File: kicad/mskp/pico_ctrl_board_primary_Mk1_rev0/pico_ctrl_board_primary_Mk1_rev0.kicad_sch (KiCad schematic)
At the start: 12 parts, among them J1 Conn_01x06_Socket, J4 USB_C_Receptacle_USB2.0, J7 OLED_128x64, J8 Conn_01x12_Socket, J9 Conn_01x03_Socket, SW3 SW_Omron_B3FS, U1 Raspberry_Pi_Pico

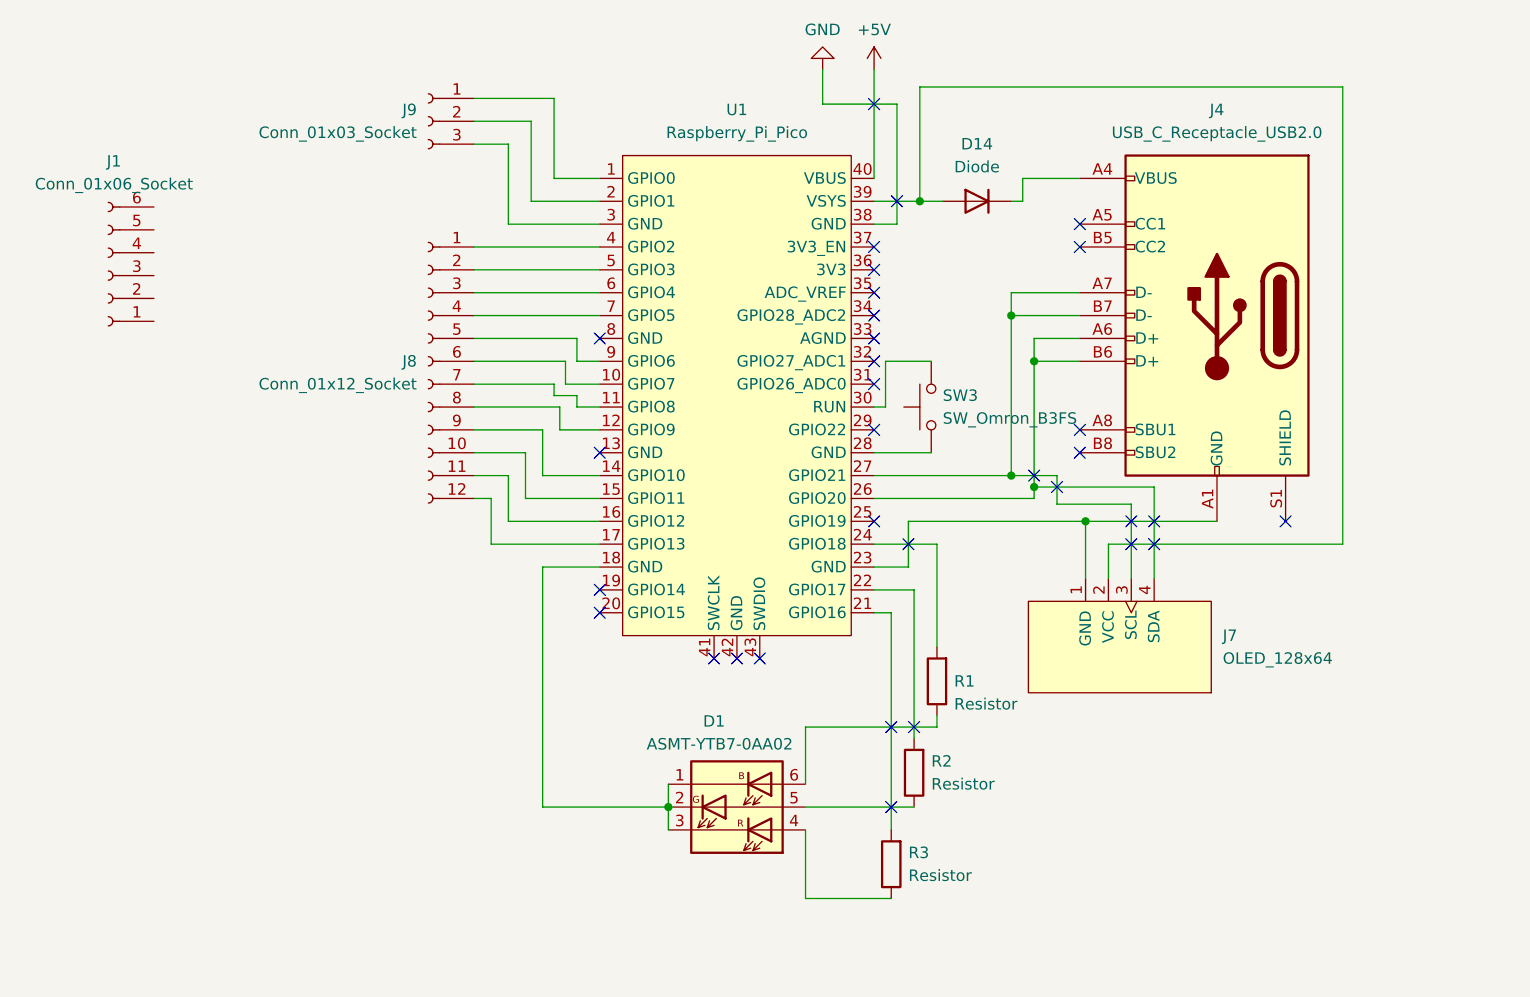
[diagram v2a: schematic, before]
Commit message: More work on pico layout and start of io shema layout
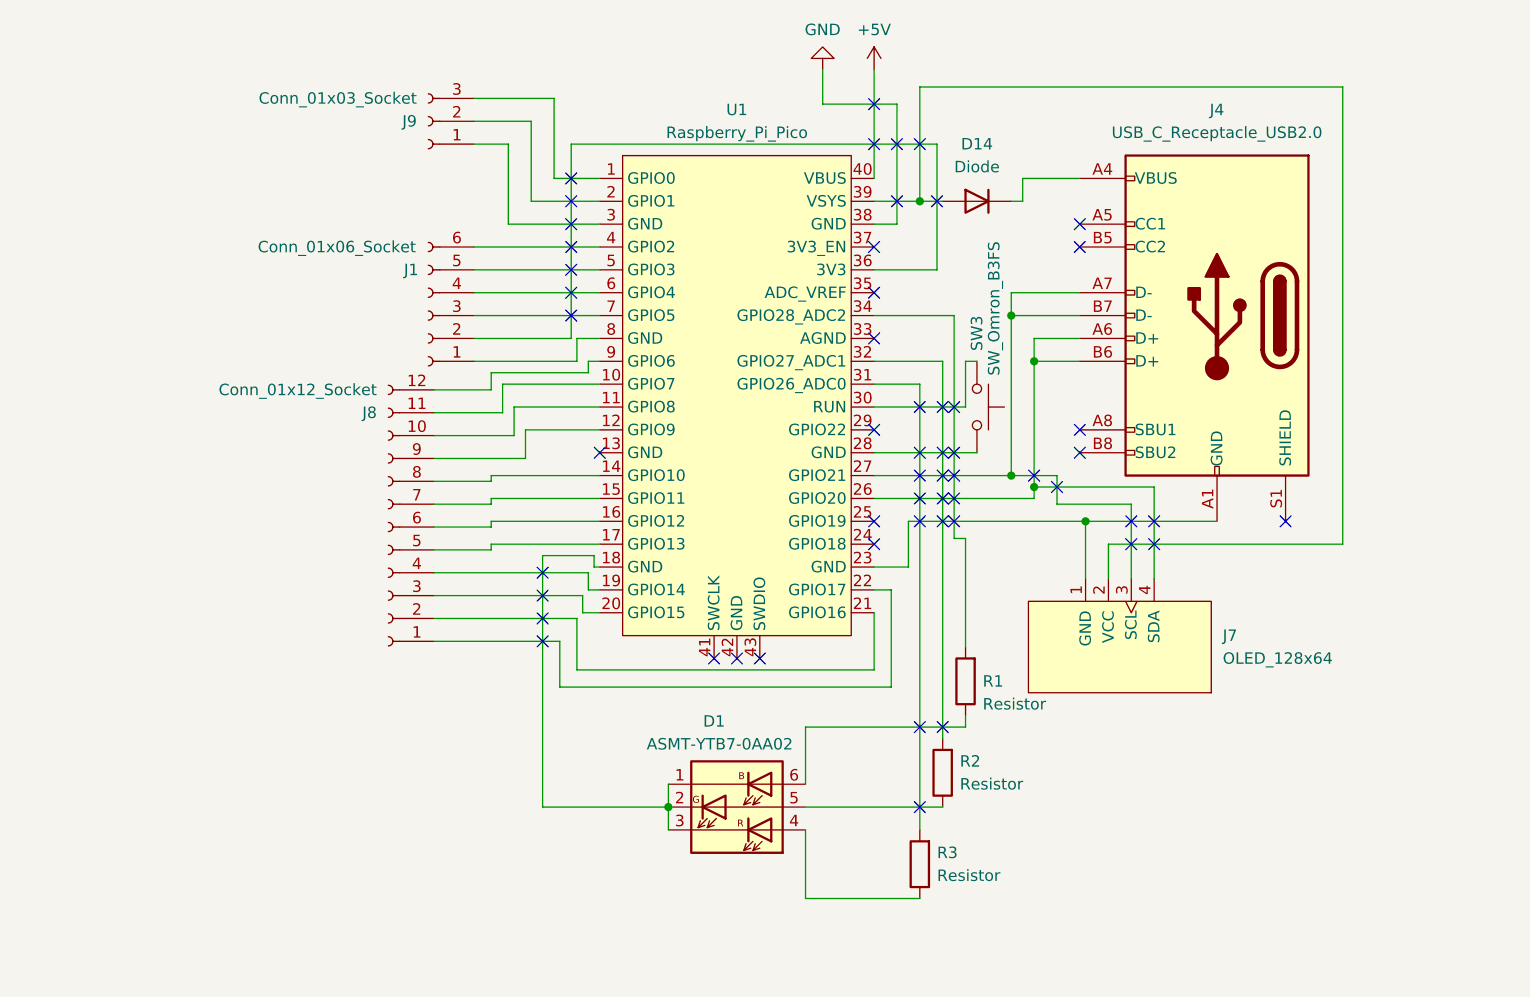
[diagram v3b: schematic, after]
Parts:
- J1: footprint (none) -> Connector_JST:JST_SH_SM06B-SRSS-TB_1x06-1MP_P1.00mm_Horizontal
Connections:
- net at U1.1 (GPIO0): now also J9.3 (Pin_3); no longer J9.1 (Pin_1)
- net at U1.10 (GPIO7): now also J8.11 (Pin_11); no longer J8.6 (Pin_6)
- net at U1.11 (GPIO8): now also J8.10 (Pin_10); no longer J8.7 (Pin_7)
- net at U1.12 (GPIO9): now also J8.9 (Pin_9); no longer J8.8 (Pin_8)
- net at U1.14 (GPIO10): now also J8.8 (Pin_8); no longer J8.9 (Pin_9)
- net at U1.15 (GPIO11): now also J8.7 (Pin_7); no longer J8.10 (Pin_10)
- net at U1.16 (GPIO12): now also J8.6 (Pin_6); no longer J8.11 (Pin_11)
- net at U1.17 (GPIO13): now also J8.5 (Pin_5); no longer J8.12 (Pin_12)
- net at U1.19 (GPIO14): now also J8.4 (Pin_4)
- net at U1.20 (GPIO15): now also J8.3 (Pin_3)
- net at U1.21 (GPIO16): now also J8.2 (Pin_2); no longer R3.2
- net at U1.22 (GPIO17): now also J8.1 (Pin_1); no longer R2.2
- net at U1.24 (GPIO18): no longer R1.2
- net at U1.3 (GND): now also J9.1 (Pin_1); no longer J9.3 (Pin_3)
- net at U1.31 (GPIO26_ADC0): now also R3.2
- net at U1.32 (GPIO27_ADC1): now also R2.2
- net at U1.34 (GPIO28_ADC2): now also R1.2
- net at U1.36 (3V3): now also J1.2 (Pin_2)
- net at U1.4 (GPIO2): now also J1.6 (Pin_6); no longer J8.1 (Pin_1)
- net at U1.5 (GPIO3): now also J1.5 (Pin_5); no longer J8.2 (Pin_2)
- net at U1.6 (GPIO4): now also J1.4 (Pin_4); no longer J8.3 (Pin_3)
- net at U1.7 (GPIO5): now also J1.3 (Pin_3); no longer J8.4 (Pin_4)
- net at U1.8 (GND): now also J1.1 (Pin_1)
- net at U1.9 (GPIO6): now also J8.12 (Pin_12); no longer J8.5 (Pin_5)
- no-connect marks 33 -> 56
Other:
- moved on the sheet: J1, J8, J9, R1, R2, R3, SW3

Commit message: Adds wiring for pico_ctrl_board_primary_Mk1_rev0
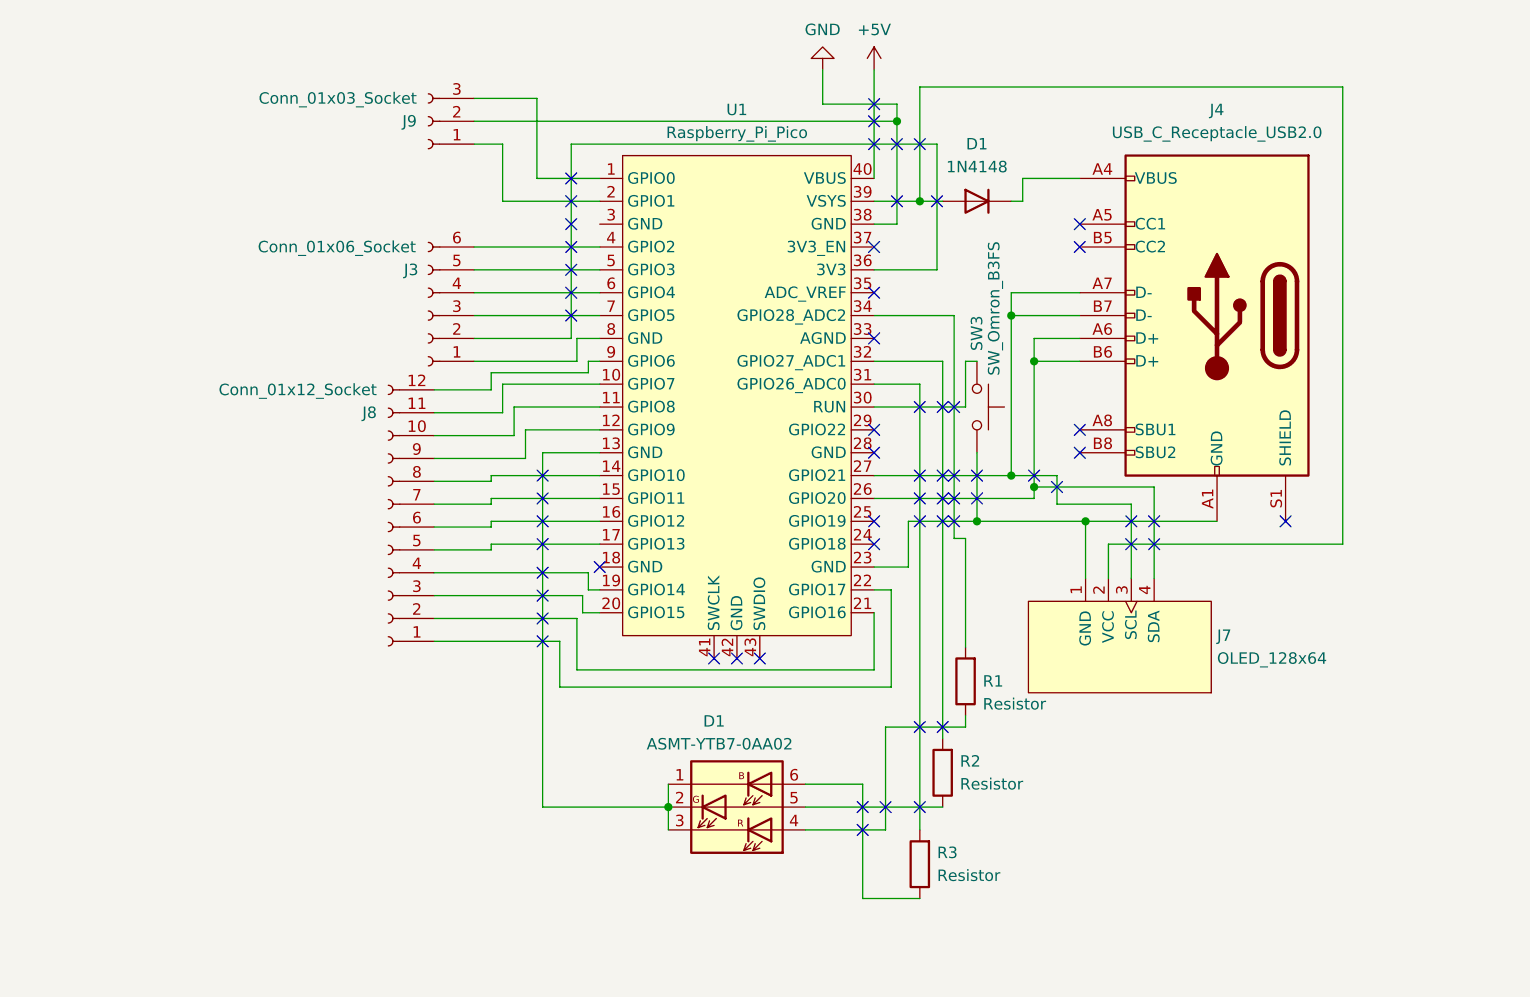
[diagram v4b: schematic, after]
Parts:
- removed D14: Diode, ScottoKeebs_Components:Diode_DO-35, symbol ScottoKeebs:Placeholder_Diode
- added D1: 1N4148, Diode_THT:D_DO-35_SOD27_P7.62mm_Horizontal, symbol Diode:1N4148
- renumbered J1 to J3
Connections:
- net GND: now also J9.2 (Pin_2)
- net at U1.13 (GND): now also D1.1 (KB), D1.2 (KG), D1.3 (KR)
- net at U1.2 (GPIO1): now also J9.1 (Pin_1); no longer J9.2 (Pin_2)
- net at J4.A1 (GND), J4.A12 (GND), J4.B1 (GND)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: now also SW3.1
- net at U1.28 (GND): no longer SW3.1
- net at U1.3 (GND): no longer J9.1 (Pin_1)
- net at J7.2 (VCC), U1.39 (VSYS): now also D1.2 (A)
- net at R3.1: now also D1.6 (AB); no longer D1.4 (AR)
- net at J4.A4 (VBUS), J4.A9 (VBUS), J4.B4 (VBUS)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: now also D1.1 (K)
- net at R1.1: now also D1.4 (AR); no longer D1.6 (AB)
- now unconnected: U1.18 (GND)
- no-connect marks 56 -> 64
